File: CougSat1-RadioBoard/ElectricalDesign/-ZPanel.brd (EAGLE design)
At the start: 96 x 96 mm, 38 parts, among them J4 ADCS, U1 AD7291, U3 AD8515

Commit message: Updated -Z Layout
Last one bad this 1 gud
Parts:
- moved C12 13.8 mm to (-2.50, 33.8), turned to 180 degrees
- moved R12 1.35 mm to (-1.05, 31.4)
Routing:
- net 3.3V: track 54.1 -> 49.1 mm
- net PD/RST: track 3.16 -> 4.20 mm
- net I2C_SDA_ADCS: track 24.6 -> 23.5 mm
- net I2C_SCL_ADCS: track 23.3 -> 22.4 mm
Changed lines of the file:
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@@
 <attribute name="VOLTAGE" value="50V" x="37.14" y="73.48" size="1.778" layer="27" rot="R90" display="off"/>
 </element>
-<element name="C12" library="CougsInSpace-Capacitors" package="1608" value="100nF 10%" x="-12.5" y="24.25" smashed="yes">
-<attribute name="NAME" x="-12.5" y="25.65" size="0.8" layer="25" font="vector" ratio="15" align="center"/>
-<attribute name="PACKAGE" value="1608" x="21.79" y="-16.39" size="1.778" layer="27" display="off"/>
-<attribute name="SKU" value="11-104A" x="21.79" y="-16.39" size="1.778" layer="27" display="off"/>
-<attribute name="TEMP" value="X7R" x="21.79" y="-16.39" size="1.778" layer="27" display="off"/>
-<attribute name="VOLTAGE" value="50V" x="21.79" y="-16.39" size="1.778" layer="27" display="off"/>
+<element name="C12" library="CougsInSpace-Capacitors" package="1608" value="100nF 10%" x="-2.5" y="33.75" smashed="yes" rot="R180">
+<attribute name="NAME" x="-2.5" y="32.35" size="0.8" layer="25" font="vector" ratio="15" rot="R180" align="center"/>
+<attribute name="PACKAGE" value="1608" x="-36.79" y="74.39" size="1.778" layer="27" rot="R180" display="off"/>
+<attribute name="SKU" value="11-104A" x="-36.79" y="74.39" size="1.778" layer="27" rot="R180" display="off"/>
+<attribute name="TEMP" value="X7R" x="-36.79" y="74.39" size="1.778" layer="27" rot="R180" display="off"/>
+<attribute name="VOLTAGE" value="50V" x="-36.79" y="74.39" size="1.778" layer="27" rot="R180" display="off"/>
 </element>
 <element name="C2" library="CougsInSpace-Capacitors" package="4028-POL" value="4.7µF 10%" x="-27.25" y="9.5" smashed="yes">
@@
 <attribute name="TEMP" value="70°C Max 2A" x="-45.45" y="20.14" size="1.778" layer="27" rot="SR270" display="off"/>
 </element>
-<element name="R12" library="CougsInSpace-Resistors" package="1608" value="1kΩ 0.1%" x="-1.55" y="32.67" smashed="yes" rot="R180">
-<attribute name="NAME" x="-1.55" y="31.27" size="0.8" layer="25" font="vector" ratio="15" rot="R180" align="center"/>
-<attribute name="PACKAGE" value="1608" x="-28.22" y="77.12" size="1.778" layer="27" rot="R180" display="off"/>
-<attribute name="POWER" value="1/8W" x="-28.22" y="77.12" size="1.778" layer="27" rot="R180" display="off"/>
-<attribute name="SKU" value="21-1001" x="-28.22" y="77.12" size="1.778" layer="27" rot="R180" display="off"/>
-<attribute name="TEMP" value="25ppm/°C" x="-28.22" y="77.12" size="1.778" layer="27" rot="R180" display="off"/>
+<element name="R12" library="CougsInSpace-Resistors" package="1608" value="1kΩ 0.1%" x="-1.05" y="31.42" smashed="yes" rot="R180">
+<attribute name="NAME" x="-1.05" y="30.02" size="0.8" layer="25" font="vector" ratio="15" rot="R180" align="center"/>
+<attribute name="PACKAGE" value="1608" x="-27.72" y="75.87" size="1.778" layer="27" rot="R180" display="off"/>
+<attribute name="POWER" value="1/8W" x="-27.72" y="75.87" size="1.778" layer="27" rot="R180" display="off"/>
+<attribute name="SKU" value="21-1001" x="-27.72" y="75.87" size="1.778" layer="27" rot="R180" display="off"/>
+<attribute name="TEMP" value="25ppm/°C" x="-27.72" y="75.87" size="1.778" layer="27" rot="R180" display="off"/>
 </element>
 <element name="R3" library="CougsInSpace-Resistors" package="1608" value="150Ω 1%" x="28" y="2.5" smashed="yes" rot="R180">
@@
 <contactref element="U1" pad="14"/>
 <contactref element="J4" pad="1"/>
-<wire x1="-16.25" y1="20" x2="-16.25" y2="25" width="0.16" layer="1"/>
-<wire x1="-16.25" y1="25" x2="-4.25" y2="37" width="0.16" layer="1"/>
-<wire x1="-4.25" y1="37" x2="-1.65" y2="37" width="0.16" layer="1"/>
+<wire x1="-16.25" y1="20" x2="-16.25" y2="23.25" width="0.16" layer="1"/>
+<wire x1="-16.25" y1="23.25" x2="-2.5" y2="37" width="0.16" layer="1"/>
+<wire x1="-2.5" y1="37" x2="-1.65" y2="37" width="0.16" layer="1"/>
 </signal>
 <signal name="I2C_SCL_ADCS">
 <contactref element="J4" pad="2"/>
 <contactref element="U1" pad="15"/>
-<wire x1="-14.75" y1="20" x2="-14.75" y2="25.75" width="0.16" layer="1"/>
-<wire x1="-4" y1="36.5" x2="-1.65" y2="36.5" width="0.16" layer="1"/>
-<wire x1="-14.75" y1="25.75" x2="-4" y2="36.5" width="0.16" layer="1"/>
+<wire x1="-14.75" y1="20" x2="-14.75" y2="24.25" width="0.16" layer="1"/>
+<wire x1="-2.5" y1="36.5" x2="-1.65" y2="36.5" width="0.16" layer="1"/>
+<wire x1="-14.75" y1="24.25" x2="-2.5" y2="36.5" width="0.16" layer="1"/>
 </signal>
 <signal name="DGND">
@@
 <contactref element="U1" pad="9"/>
 <wire x1="-11.75" y1="20" x2="-11.75" y2="22.5" width="0.16" layer="1"/>
-<wire x1="-11.75" y1="24.25" x2="-11.75" y2="22.5" width="0.16" layer="1"/>
 <wire x1="-0.25" y1="39.4" x2="-0.25" y2="40.25" width="0.16" layer="1"/>
 <wire x1="-0.25" y1="40.25" x2="-1" y2="41" width="0.16" layer="1"/>
 <wire x1="-1" y1="41" x2="-1" y2="42.25" width="0.16" layer="1"/>
-<wire x1="-11.75" y1="24.25" x2="-11.75" y2="25.5" width="0.16" layer="1"/>
-<wire x1="-11.75" y1="25.5" x2="-6" y2="31.25" width="0.16" layer="1"/>
-<wire x1="-2.75" y1="34.5" x2="0.25" y2="37.5" width="0.16" layer="1"/>
 <wire x1="0.25" y1="37.5" x2="-0.25" y2="38" width="0.16" layer="1"/>
 <wire x1="-0.25" y1="38" x2="-0.25" y2="39.4" width="0.16" layer="1"/>
 <wire x1="-1.65" y1="37.5" x2="0.25" y2="37.5" width="0.16" layer="1"/>
-<wire x1="-6" y1="31.25" x2="-6" y2="32.25" width="0.16" layer="1"/>
-<wire x1="-6" y1="32.25" x2="-3.75" y2="34.5" width="0.16" layer="1"/>
-<wire x1="-3.75" y1="34.5" x2="-2.75" y2="34.5" width="0.16" layer="1"/>
 <contactref element="R1" pad="2"/>
 <via x="-11.75" y="22.5" extent="1-16" drill="0.35"/>
@@
 <wire x1="-31.5" y1="23.75" x2="-30.25" y2="22.5" width="0.16" layer="1"/>
 <via x="-30.25" y="22.5" extent="1-16" drill="0.35"/>
+<wire x1="-3.25" y1="34" x2="-3.25" y2="33.75" width="0.16" layer="1"/>
+<wire x1="0.25" y1="37.5" x2="-3.25" y2="34" width="0.16" layer="1"/>
+<wire x1="-11.75" y1="22.5" x2="-11.75" y2="26.25" width="0.16" layer="1"/>
+<wire x1="-11.75" y1="26.25" x2="-4.25" y2="33.75" width="0.16" layer="1"/>
+<wire x1="-4.25" y1="33.75" x2="-3.25" y2="33.75" width="0.16" layer="1"/>
 </signal>
 <signal name="AGND">
@@
 <wire x1="-15.75" y1="17.25" x2="-13.25" y2="19.75" width="0.16" layer="1"/>
 <wire x1="-13.25" y1="19.75" x2="-13.25" y2="20" width="0.16" layer="1"/>
-<wire x1="-13.25" y1="20" x2="-13.25" y2="24.25" width="0.16" layer="1"/>
 <wire x1="-0.75" y1="35.6" x2="-0.75" y2="34.75" width="0.16" layer="1"/>
-<wire x1="-2.3" y1="33.2" x2="-2.3" y2="32.67" width="0.16" layer="1"/>
-<wire x1="-0.75" y1="34.75" x2="-2.3" y2="33.2" width="0.16" layer="1"/>
-<wire x1="-13.25" y1="20" x2="-11" y2="17.75" width="0.16" layer="1"/>
-<wire x1="-11" y1="17.75" x2="-10.25" y2="17.75" width="0.16" layer="1"/>
-<wire x1="-10.25" y1="17.75" x2="-2.3" y2="25.7" width="0.16" layer="1"/>
-<wire x1="-2.3" y1="25.7" x2="-2.3" y2="32.67" width="0.16" layer="1"/>
+<wire x1="-1.8" y1="33.7" x2="-1.8" y2="31.42" width="0.16" layer="1"/>
+<wire x1="-0.75" y1="34.75" x2="-1.75" y2="33.75" width="0.16" layer="1"/>
+<wire x1="-1.75" y1="33.75" x2="-1.8" y2="33.7" width="0.16" layer="1"/>
 <wire x1="-4.5" y1="38.5" x2="-1.65" y2="38.5" width="0.16" layer="1"/>
-<wire x1="-2.3" y1="32.67" x2="-3.92" y2="32.67" width="0.16" layer="1"/>
-<wire x1="-3.92" y1="32.67" x2="-4.274515625" y2="33.024515625" width="0.16" layer="1"/>
-<via x="-4.274515625" y="33.024515625" extent="1-16" drill="0.35"/>
-<wire x1="-4.274515625" y1="33.024515625" x2="-6.5" y2="35.25" width="0.16" layer="16"/>
-<wire x1="-6.5" y1="35.25" x2="-6.5" y2="36" width="0.16" layer="16"/>
+<wire x1="-1.8" y1="31.42" x2="-3.17" y2="31.42" width="0.16" layer="1"/>
+<wire x1="-3.17" y1="31.42" x2="-4.024515625" y2="32.274515625" width="0.16" layer="1"/>
+<via x="-4.024515625" y="32.274515625" extent="1-16" drill="0.35"/>
+<wire x1="-4.024515625" y1="32.274515625" x2="-6.5" y2="34.75" width="0.16" layer="16"/>
+<wire x1="-6.5" y1="34.75" x2="-6.5" y2="36" width="0.16" layer="16"/>
 <via x="-6.5" y="36" extent="1-16" drill="0.35"/>
 <wire x1="-6.5" y1="36" x2="-6.5" y2="36.5" width="0.16" layer="1"/>
 <wire x1="-6.5" y1="36.5" x2="-4.5" y2="38.5" width="0.16" layer="1"/>
+<wire x1="-1.8" y1="31.42" x2="-1.8" y2="27.95" width="0.16" layer="1"/>
+<wire x1="-1.8" y1="27.95" x2="-10.75" y2="19" width="0.16" layer="1"/>
+<wire x1="-10.75" y1="19" x2="-12.25" y2="19" width="0.16" layer="1"/>
+<wire x1="-12.25" y1="19" x2="-13.25" y2="20" width="0.16" layer="1"/>
 </signal>
 <signal name="AVDD">
@@
 <contactref element="U1" pad="17"/>
 <wire x1="-0.25" y1="34.6" x2="-0.25" y2="35.6" width="0.16" layer="1"/>
-<wire x1="-0.8" y1="32.67" x2="-0.8" y2="34.05" width="0.16" layer="1"/>
-<wire x1="-0.8" y1="34.05" x2="-0.25" y2="34.6" width="0.16" layer="1"/>
+<wire x1="-0.3" y1="31.42" x2="-0.3" y2="34.55" width="0.16" layer="1"/>
+<wire x1="-0.3" y1="34.55" x2="-0.25" y2="34.6" width="0.16" layer="1"/>
 </signal>
 <signal name="VREF">
@@
 <wire x1="-27.25" y1="28" x2="-25.75" y2="26.5" width="0.16" layer="1"/>
 <via x="-25.75" y="26.5" extent="1-16" drill="0.35"/>
-<wire x1="-25.75" y1="26.5" x2="-10" y2="26.5" width="0.16" layer="16"/>
-<wire x1="-10" y1="26.5" x2="2.5" y2="39" width="0.16" layer="16"/>
+<wire x1="-25.75" y1="26.5" x2="-8.75" y2="26.5" width="0.16" layer="16"/>
+<wire x1="-8.75" y1="26.5" x2="3.75" y2="39" width="0.16" layer="16"/>
 <wire x1="2.15" y1="38.5" x2="3.75" y2="38.5" width="0.16" layer="1"/>
 <wire x1="3.75" y1="38.5" x2="4.25" y2="39" width="0.16" layer="1"/>
-<wire x1="2.5" y1="39" x2="4.25" y2="39" width="0.16" layer="16"/>
+<wire x1="3.75" y1="39" x2="4.25" y2="39" width="0.16" layer="16"/>
 <via x="4.25" y="39" extent="1-16" drill="0.35"/>
 <wire x1="6.73" y1="41.11" x2="6.75" y2="41.09" width="0.16" layer="1"/>

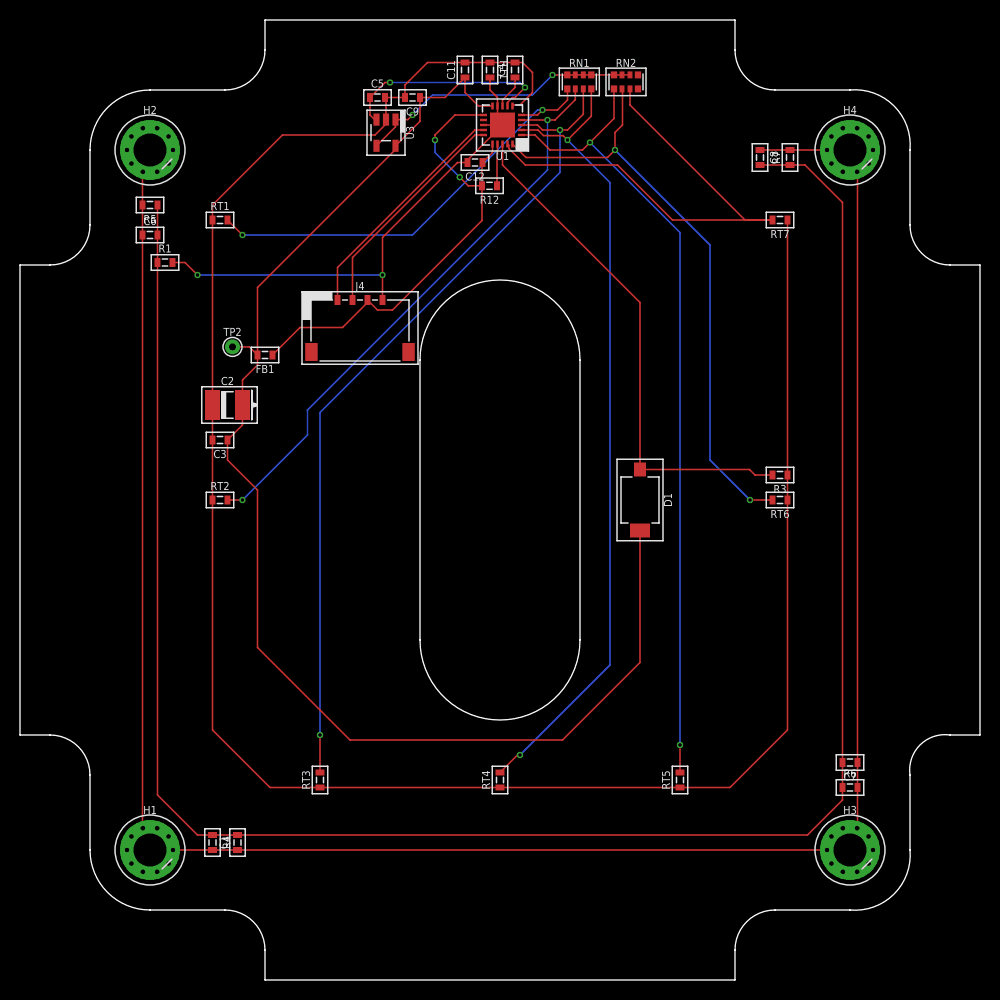
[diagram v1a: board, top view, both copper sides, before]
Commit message: Update -ZPanel.brd
- Fixed layout concerning decoupling caps and other space inconsistencies
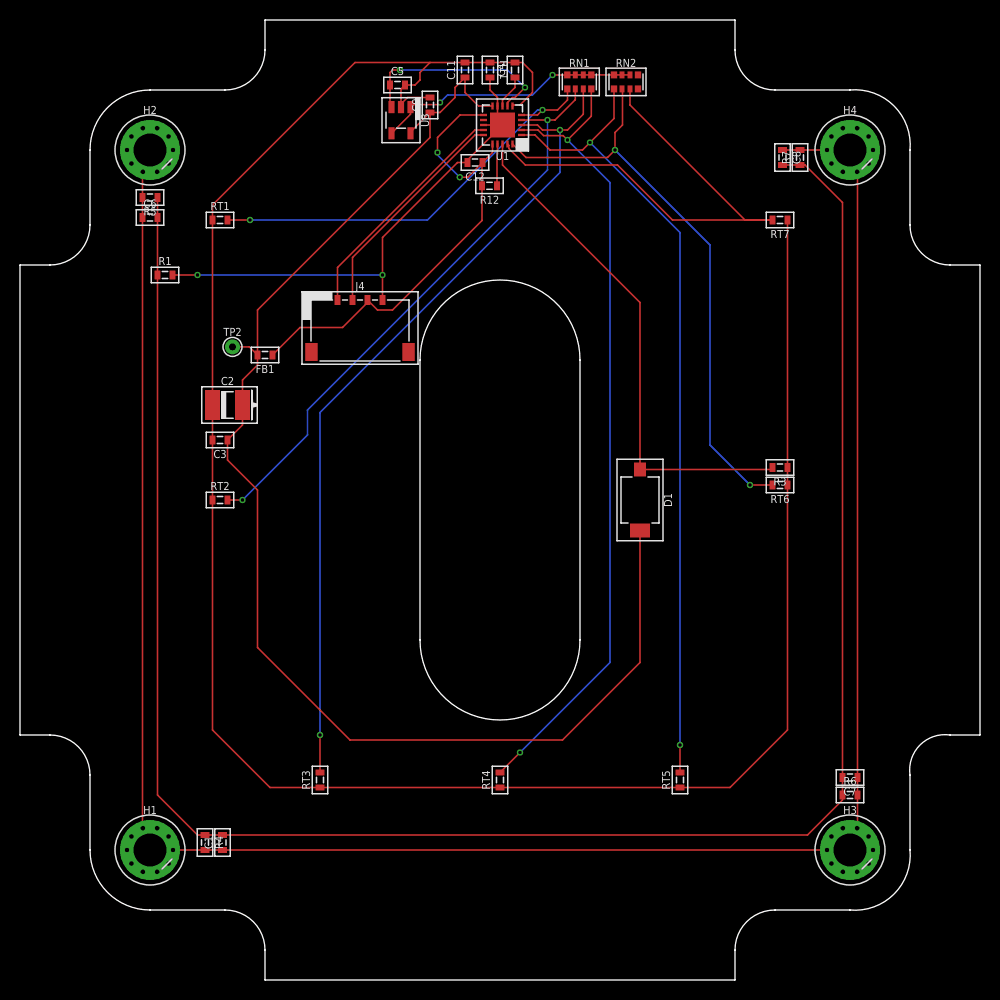
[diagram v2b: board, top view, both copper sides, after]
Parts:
- moved C5 2.36 mm to (-10.2, 41.5)
- moved C8 2.25 mm to (28.2, 34.2)
- moved U3 1.95 mm to (-9.90, 38.0)
- moved C9 1.90 mm to (-7.00, 39.5), turned to 90 degrees
- moved C6 1.75 mm to (-35.0, 28.2)
- moved C1 1.50 mm to (-27.8, -34.2)
- moved C7 1.50 mm to (35.0, -27.8)
- moved RT6 1.50 mm to (28.0, 1.50)
- moved R1 1.25 mm to (-33.5, 22.5)
- moved R7 1.00 mm to (30.0, 34.2)
- moved R3 0.75 mm to (28.0, 3.25)
- moved R4 0.75 mm to (-29.5, -34.2)
- moved R5 0.75 mm to (-35.0, 30.2)
- moved R6 0.75 mm to (35.0, -29.5)
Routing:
- net AGND: track 211.1 -> 218.1 mm
- net CHASSIS: track 306.2 -> 304.0 mm
- net AVREF: track 28.7 -> 26.7 mm
- net AVDD: track 135.7 -> 137.7 mm
- net THERM-5: track 60.4 -> 58.9 mm
- net PGND: track 200.2 -> 198.7 mm
- net THERM-0: track 43.6 -> 42.4 mm
- net VREF: track 21.6 -> 20.7 mm
- net DGND: track 51.7 -> 51.2 mm

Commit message: Update -ZPanel.brd
Added cross hatching and moved the reference designators into visible spots. Also fixed some space inconsistencies again.
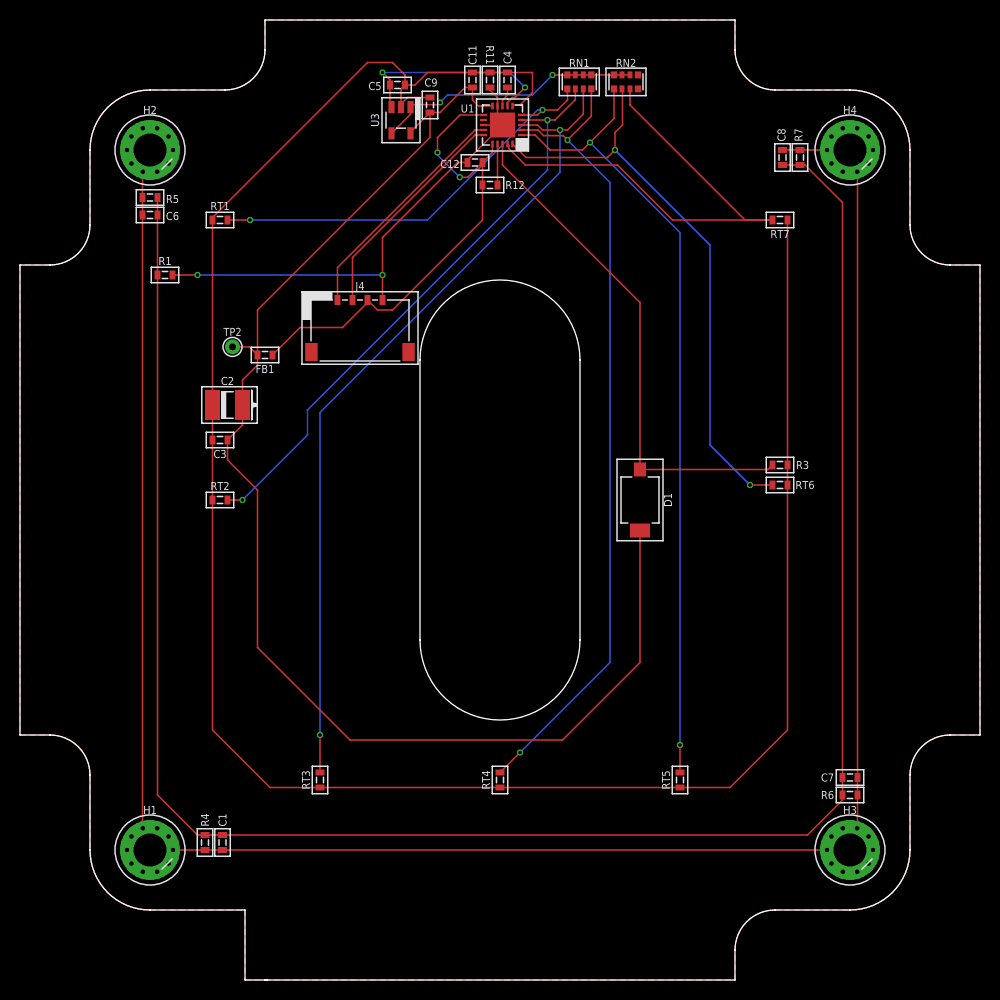
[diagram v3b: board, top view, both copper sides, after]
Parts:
- moved C11 1.25 mm to (-2.75, 42.0)
- moved C4 1.25 mm to (0.75, 42.0)
- moved R11 1.00 mm to (-1.00, 42.0)
- moved C6 0.25 mm to (-35.0, 28.5)
- moved R3 0.25 mm to (28.0, 3.50)
- moved R12 0.09 mm to (-1.00, 31.5)
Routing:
- net AGND: track 218.1 -> 215.1 mm
- net AVDD: track 137.7 -> 136.1 mm
- net DCAP: track 3.37 -> 2.06 mm
- net DGND: track 51.2 -> 50.2 mm
- net VREF: track 20.7 -> 21.5 mm
- added copper zone on layer 1, net HATCH
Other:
- outline, holes or cut-outs redrawn
